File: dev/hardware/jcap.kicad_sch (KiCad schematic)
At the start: 4 parts, among them U1 P8X32A-D40, U2 P8X32A-D40, Y1 Crystal, Y2 Crystal

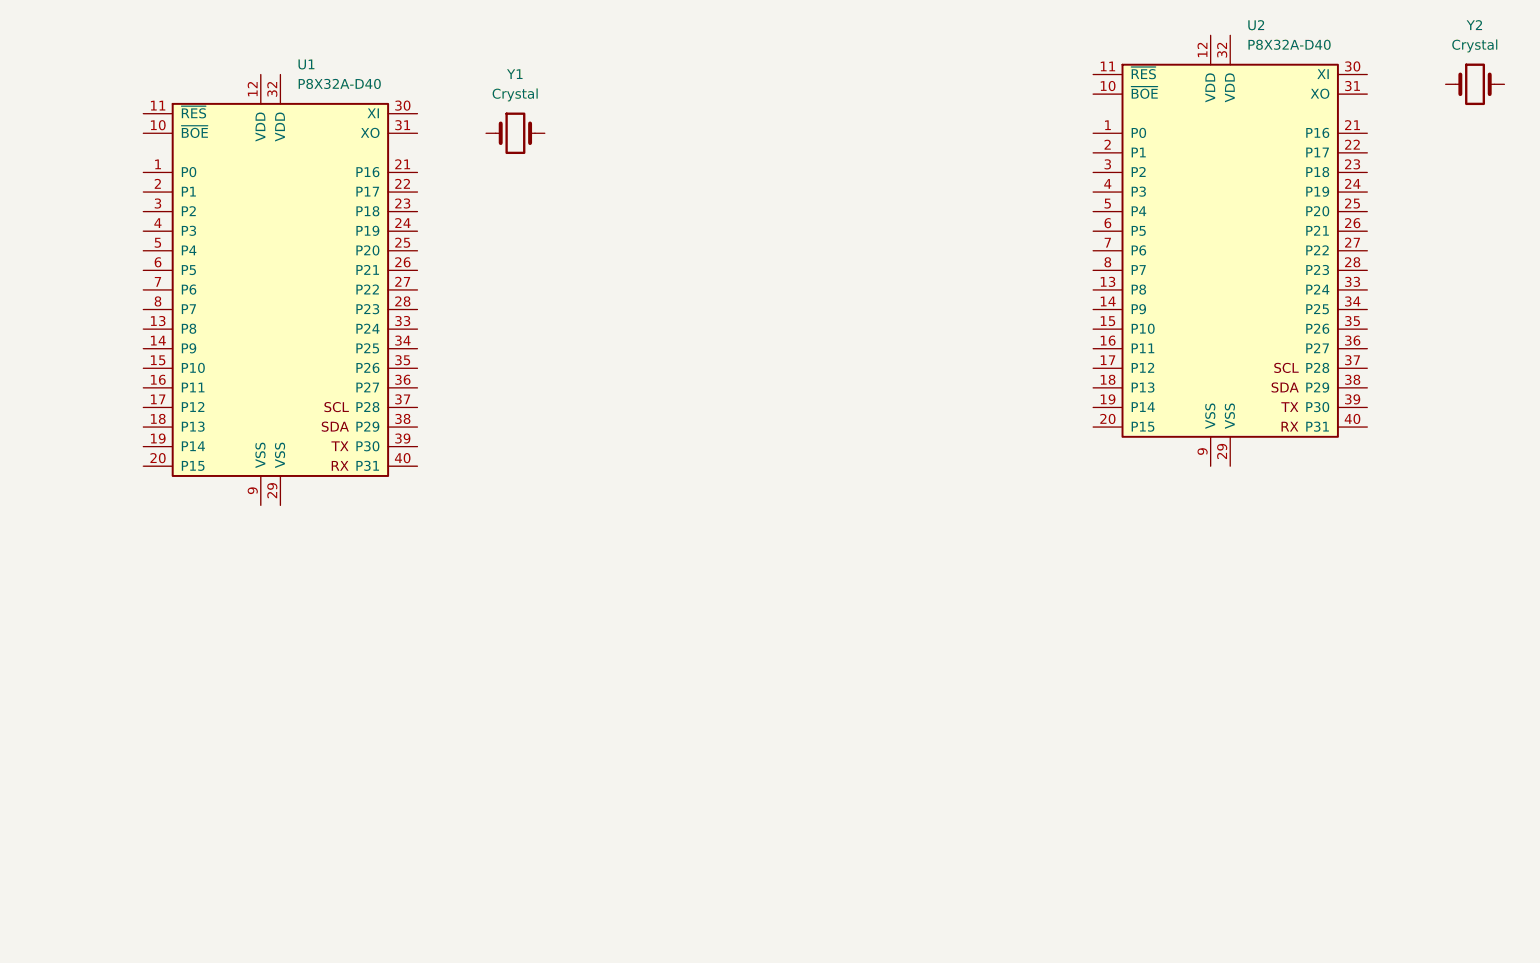
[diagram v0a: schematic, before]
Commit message: Started developing sheet hierarchy
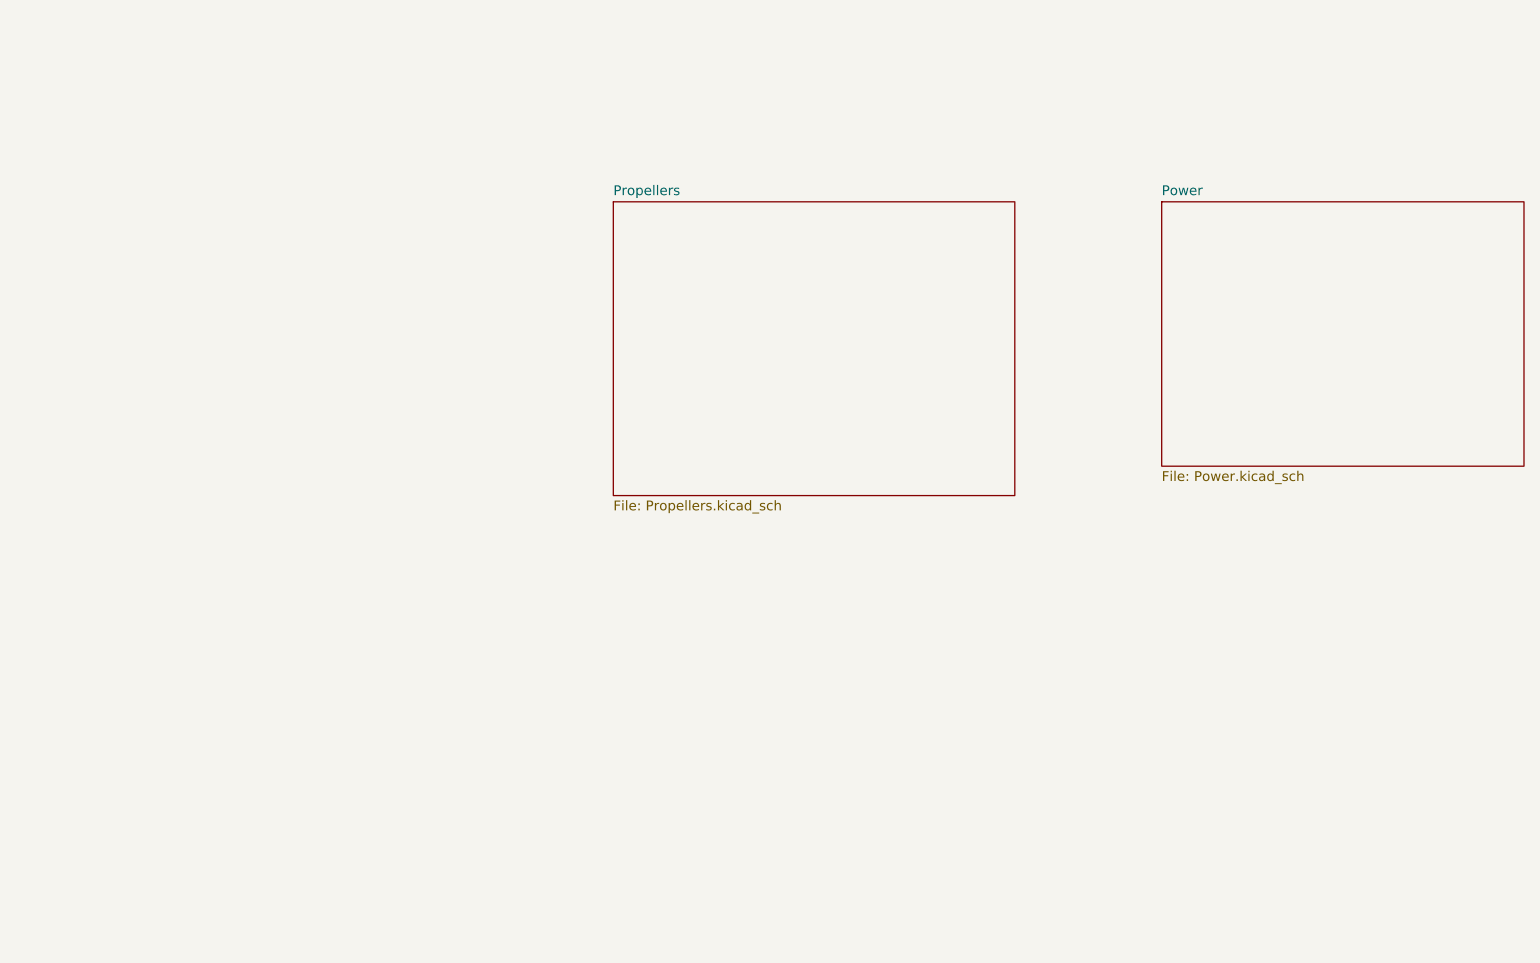
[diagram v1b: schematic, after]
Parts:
- removed U1, U2: P8X32A-D40, Package_DIP:DIP-40_W15.24mm_Socket, symbol MCU_Parallax:P8X32A-D40
- removed Y1: Crystal, Crystal:Crystal_HC49-U_Vertical, symbol Device:Crystal
- removed Y2: Crystal, symbol Device:Crystal
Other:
- added sheet Power (Power.kicad_sch)
- added sheet Propellers (Propellers.kicad_sch)
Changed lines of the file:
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@@
     (comment 4 "Name: Connor Spangler")
   )
-  (symbol (lib_id "MCU_Parallax:P8X32A-D40") (at 190.5 66.04 0) (unit 1)
-    (in_bom yes) (on_board yes) (dnp no) (fields_autoplaced)
-    (property "Reference" "U2" (at 192.6941 36.83 0)
-      (effects (font (size 1.27 1.27)) (justify left))
+  (sheet (at 110.49 59.69) (size 52.07 38.1) (fields_autoplaced)
+    (stroke (width 0.1524) (type solid))
+    (fill (color 0 0 0 0.0000))
+    (property "Sheetname" "Propellers" (at 110.49 58.9784 0)
+      (effects (font (size 1.27 1.27)) (justify left bottom))
     )
-    (property "Value" "P8X32A-D40" (at 192.6941 39.37 0)
-      (effects (font (size 1.27 1.27)) (justify left))
+    (property "Sheetfile" "Propellers.kicad_sch" (at 110.49 98.3746 0)
+      (effects (font (size 1.27 1.27)) (justify left top))
     )
-    (property "Footprint" "Package_DIP:DIP-40_W15.24mm_Socket" (at 190.5 35.56 0)
-      (effects (font (size 1.27 1.27)) hide)
-    )
-    (property "Datasheet" "https://www.parallax.com/sites/default/files/downloads/P8X32A-Propeller-Datasheet-v1.4.0_0.pdf" (at 190.5 66.04 0)
-      (effects (font (size 1.27 1.27)) hide)
-    )
-    (pin "1")
-    (pin "10")
-    (pin "11")
-    (pin "12")
-    (pin "13")
-    (pin "14")
-    (pin "15")
-    (pin "16")
-    (pin "17")
-    (pin "18")
-    (pin "19")
-    (pin "2")
-    (pin "20")
-    (pin "21")
-    (pin "22")
-    (pin "23")
-    (pin "24")
-    (pin "25")
-    (pin "26")
-    (pin "27")
-    (pin "28")
-    (pin "29")
-    (pin "3")
-    (pin "30")
-    (pin "31")
-    (pin "32")
-    (pin "33")
-    (pin "34")
-    (pin "35")
-    (pin "36")
-    (pin "37")
-    (pin "38")
-    (pin "39")
-    (pin "4")
-    (pin "40")
-    (pin "5")
-    (pin "6")
-    (pin "7")
-    (pin "8")
-    (pin "9")
     (instances
       (project "jcap"
-        (path "/7fc25e9e-3600-419b-89ef-b962e4e374c1"
-          (reference "U2") (unit 1)
-        )
+        (path "/7fc25e9e-3600-419b-89ef-b962e4e374c1" (page "2"))
       )
     )
   )
-  (symbol (lib_id "MCU_Parallax:P8X32A-D40") (at 67.31 71.12 0) (unit 1)
-    (in_bom yes) (on_board yes) (dnp no) (fields_autoplaced)
-    (property "Reference" "U1" (at 69.5041 41.91 0)
-      (effects (font (size 1.27 1.27)) (justify left))
+  (sheet (at 181.61 59.69) (size 46.99 34.29) (fields_autoplaced)
+    (stroke (width 0.1524) (type solid))
+    (fill (color 0 0 0 0.0000))
+    (property "Sheetname" "Power" (at 181.61 58.9784 0)
+      (effects (font (size 1.27 1.27)) (justify left bottom))
     )
-    (property "Value" "P8X32A-D40" (at 69.5041 44.45 0)
-      (effects (font (size 1.27 1.27)) (justify left))
+    (property "Sheetfile" "Power.kicad_sch" (at 181.61 94.5646 0)
+      (effects (font (size 1.27 1.27)) (justify left top))
     )
-    (property "Footprint" "Package_DIP:DIP-40_W15.24mm_Socket" (at 67.31 40.64 0)
-      (effects (font (size 1.27 1.27)) hide)
-    )
-    (property "Datasheet" "https://www.parallax.com/sites/default/files/downloads/P8X32A-Propeller-Datasheet-v1.4.0_0.pdf" (at 67.31 71.12 0)
-      (effects (font (size 1.27 1.27)) hide)
-    )
-    (pin "1")
-    (pin "10")
-    (pin "11")
-    (pin "12")
-    (pin "13")
-    (pin "14")
-    (pin "15")
-    (pin "16")
-    (pin "17")
-    (pin "18")
-    (pin "19")
-    (pin "2")
-    (pin "20")
-    (pin "21")
-    (pin "22")
-    (pin "23")
-    (pin "24")
-    (pin "25")
-    (pin "26")
-    (pin "27")
-    (pin "28")
-    (pin "29")
-    (pin "3")
-    (pin "30")
-    (pin "31")
-    (pin "32")
-    (pin "33")
-    (pin "34")
-    (pin "35")
-    (pin "36")
-    (pin "37")
-    (pin "38")
-    (pin "39")
-    (pin "4")
-    (pin "40")
-    (pin "5")
-    (pin "6")
-    (pin "7")
-    (pin "8")
-    (pin "9")
     (instances
       (project "jcap"
-        (path "/7fc25e9e-3600-419b-89ef-b962e4e374c1"
-          (reference "U1") (unit 1)
-        )
+        (path "/7fc25e9e-3600-419b-89ef-b962e4e374c1" (page "3"))
       )
     )
-  )
-  (symbol (lib_id "Device:Crystal") (at 222.25 44.45 0) (unit 1)
-    (in_bom yes) (on_board yes) (dnp no) (fields_autoplaced)
-    (property "Reference" "Y2" (at 222.25 36.83 0)
-      (effects (font (size 1.27 1.27)))
-    )
-    (property "Value" "Crystal" (at 222.25 39.37 0)
-      (effects (font (size 1.27 1.27)))
-    )
-    (property "Footprint" "" (at 222.25 44.45 0)
-      (effects (font (size 1.27 1.27)) hide)
-    )
-    (property "Datasheet" "~" (at 222.25 44.45 0)
-      (effects (font (size 1.27 1.27)) hide)
-    )
-    (pin "1")
-    (pin "2")
-    (instances
-      (project "jcap"
-        (path "/7fc25e9e-3600-419b-89ef-b962e4e374c1"
-          (reference "Y2") (unit 1)
-        )
-      )
-    )
-  )
-  (symbol (lib_id "Device:Crystal") (at 97.79 50.8 0) (unit 1)
-    (in_bom yes) (on_board yes) (dnp no) (fields_autoplaced)
-    (property "Reference" "Y1" (at 97.79 43.18 0)
-      (effects (font (size 1.27 1.27)))
-    )
-    (property "Value" "Crystal" (at 97.79 45.72 0)
-      (effects (font (size 1.27 1.27)))
-    )
-    (property "Footprint" "Crystal:Crystal_HC49-U_Vertical" (at 97.79 50.8 0)
-      (effects (font (size 1.27 1.27)) hide)
-    )
-    (property "Datasheet" "~" (at 97.79 50.8 0)
-      (effects (font (size 1.27 1.27)) hide)
-    )
-    (pin "1")
-    (pin "2")
-    (instances
-      (project "jcap"
-        (path "/7fc25e9e-3600-419b-89ef-b962e4e374c1"
-          (reference "Y1") (unit 1)
-        )
-      )
-    )

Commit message: Continued developing JCAP schematic
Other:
- added sheet EEPROM (EEPROM.kicad_sch)
- added sheet VGA_DAC (VGA_DAC.kicad_sch)
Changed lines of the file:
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@@
+    )
+  )
+  (sheet (at 33.02 59.69) (size 48.26 34.29) (fields_autoplaced)
+    (stroke (width 0.1524) (type solid))
+    (fill (color 0 0 0 0.0000))
+    (property "Sheetname" "VGA_DAC" (at 33.02 58.9784 0)
+      (effects (font (size 1.27 1.27)) (justify left bottom))
+    )
+    (property "Sheetfile" "VGA_DAC.kicad_sch" (at 33.02 94.5646 0)
+      (effects (font (size 1.27 1.27)) (justify left top))
+    )
+    (instances
+      (project "jcap"
+        (path "/7fc25e9e-3600-419b-89ef-b962e4e374c1" (page "5"))
+      )
     )
   )
@@
       )
     )
+  )
+  (sheet (at 86.36 124.46) (size 33.02 29.21) (fields_autoplaced)
+    (stroke (width 0.1524) (type solid))
+    (fill (color 0 0 0 0.0000))
+    (property "Sheetname" "EEPROM" (at 86.36 123.7484 0)
+      (effects (font (size 1.27 1.27)) (justify left bottom))
+    )
+    (property "Sheetfile" "EEPROM.kicad_sch" (at 86.36 154.2546 0)
+      (effects (font (size 1.27 1.27)) (justify left top))
+    )
+    (instances
+      (project "jcap"
+        (path "/7fc25e9e-3600-419b-89ef-b962e4e374c1" (page "4"))
+      )
+    )

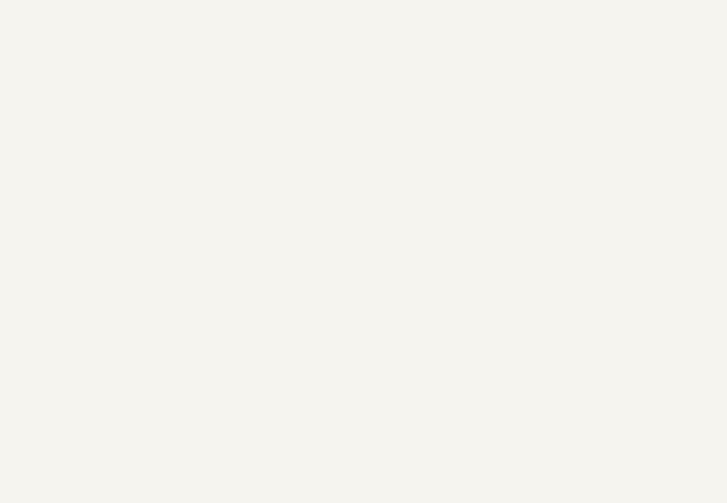
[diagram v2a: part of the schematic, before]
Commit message: Finalized initial schematic
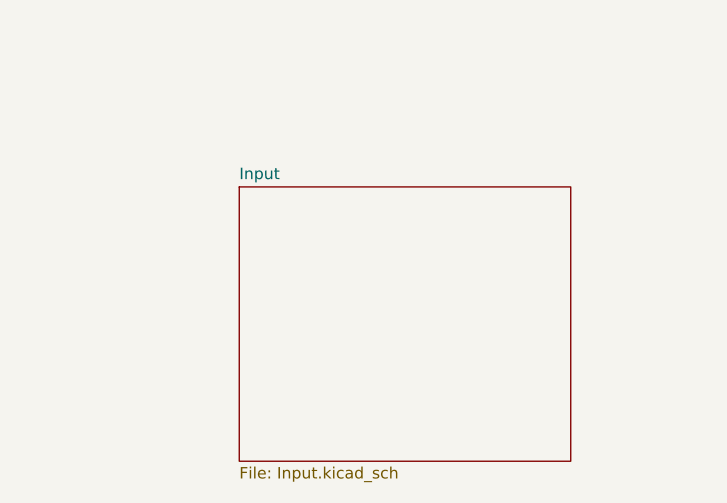
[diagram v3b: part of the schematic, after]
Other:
- added sheet Input (Input.kicad_sch)
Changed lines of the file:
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@@
+    )
+  )
+  (sheet (at 176.53 123.19) (size 36.83 30.48) (fields_autoplaced)
+    (stroke (width 0.1524) (type solid))
+    (fill (color 0 0 0 0.0000))
+    (property "Sheetname" "Input" (at 176.53 122.4784 0)
+      (effects (font (size 1.27 1.27)) (justify left bottom))
+    )
+    (property "Sheetfile" "Input.kicad_sch" (at 176.53 154.2546 0)
+      (effects (font (size 1.27 1.27)) (justify left top))
+    )
+    (instances
+      (project "jcap"
+        (path "/7fc25e9e-3600-419b-89ef-b962e4e374c1" (page "6"))
+      )
     )
   )
